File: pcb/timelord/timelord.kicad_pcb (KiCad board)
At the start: 4 copper layers, 65 x 56.5 mm, 16 parts, among them J1 Raspberry_Pi_4, J2 OLED, J3 SMA, J4 EXTERNAL, U1 NEO-F10T

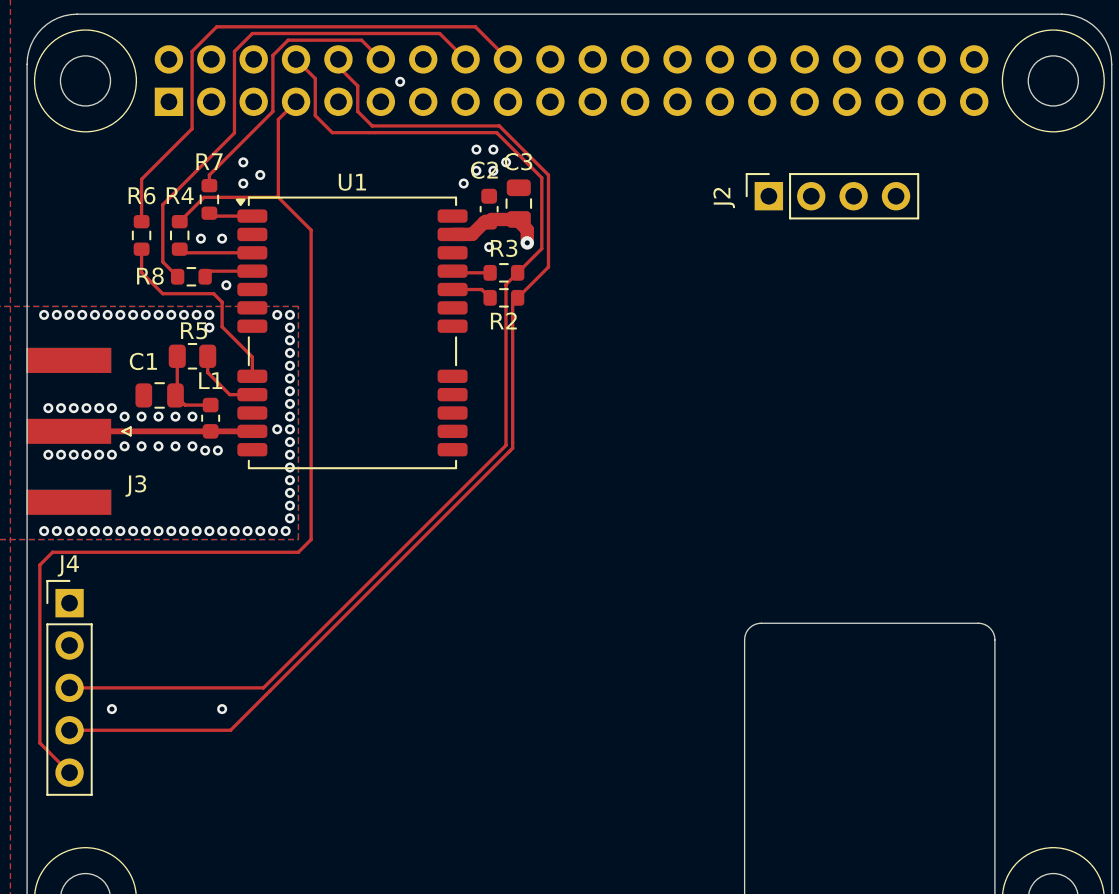
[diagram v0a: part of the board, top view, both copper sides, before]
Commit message: Add external I2C RTC
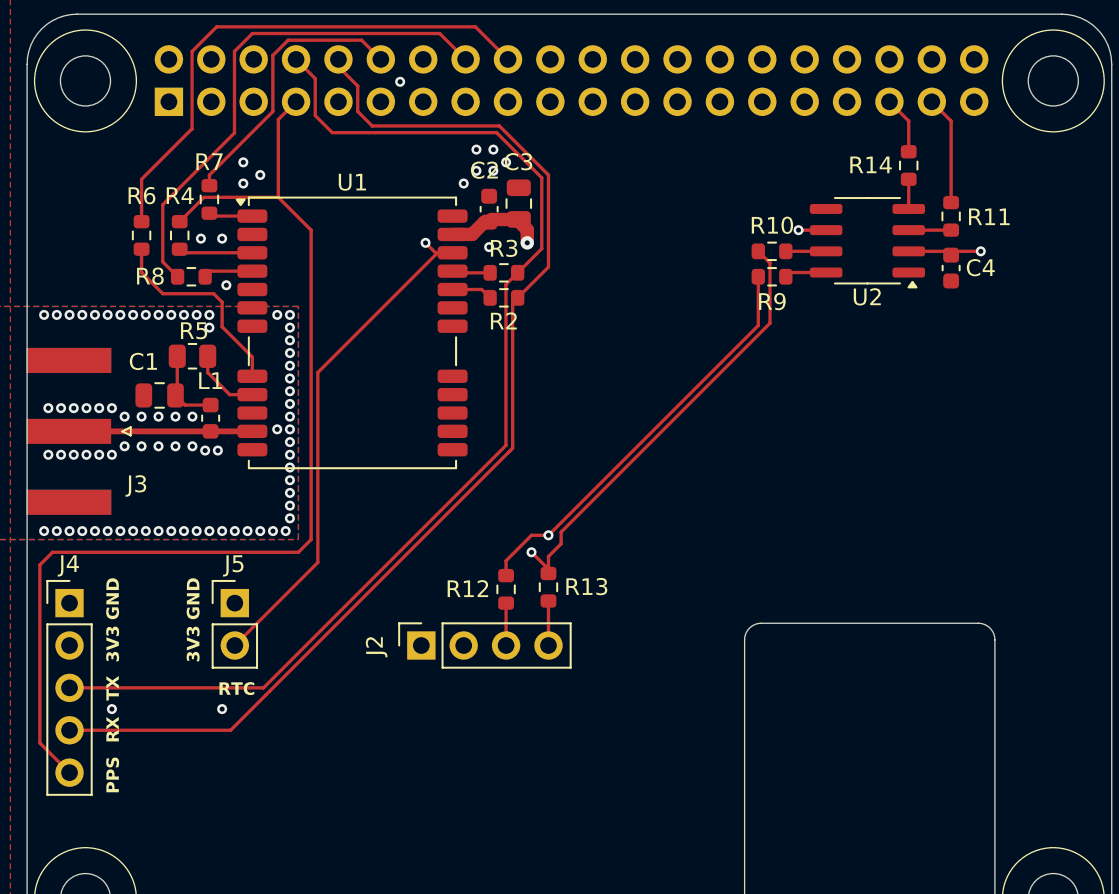
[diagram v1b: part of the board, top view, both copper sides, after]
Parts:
- added C4: 1u, Capacitor_SMD:C_0603_1608Metric, F.Cu at (214.4, 46.2)
- added J5: BCKP_PWR, Connector_PinHeader_2.54mm:PinHeader_1x02_P2.54mm_Vertical, F.Cu at (171.4, 66.3)
- added R10: 33, Resistor_SMD:R_0603_1608Metric, F.Cu at (203.6, 45.2)
- added R11: 33, Resistor_SMD:R_0603_1608Metric, F.Cu at (214.4, 43.1)
- added R12: 33, Resistor_SMD:R_0603_1608Metric, F.Cu at (187.7, 65.5)
- added R13: 33, Resistor_SMD:R_0603_1608Metric, F.Cu at (190.2, 65.3)
- added R14: 33, Resistor_SMD:R_0603_1608Metric, F.Cu at (211.8, 40.1)
- added R9: 33, Resistor_SMD:R_0603_1608Metric, F.Cu at (203.6, 46.7)
- added U2: DS3231MZ, Package_SO:SOIC-8_3.9x4.9mm_P1.27mm, F.Cu at (209.4, 44.6)
- moved J2 34.0 mm to (182.6, 68.8)
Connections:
- J1 pad 35: unconnected-(J1-GPIO19/SPI1_MISO/PCM_FS-Pad35) -> RTC_RESET
- J1 pad 37: unconnected-(J1-GPIO26/SDIO_DAT2-Pad37) -> PPS_RTC
- J2 pad 3: SCL -> Net-(J2-Pin_3)
- J2 pad 4: SDA -> Net-(J2-Pin_4)
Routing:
- net VCC_BCKP: track 0.00 -> 55.7 mm, vias 0 -> 2
- net SCL: track 40.2 -> 58.1 mm, vias 0 -> 1
- net SDA: track 44.9 -> 62.5 mm, vias 0 -> 1
- net PPS_RTC: track 0.00 -> 6.52 mm
- net +3.3V: track 5.88 -> 10.2 mm, vias 1 -> 2
- net RTC_RESET: track 0.00 -> 3.47 mm
- net Net-(J2-Pin_4): track 0.00 -> 2.67 mm
- net Net-(J2-Pin_3): track 0.00 -> 2.54 mm
- net Net-(U2-~{INT}/SQW): track 0.00 -> 2.54 mm
- net Net-(U2-SCL): track 0.00 -> 2.52 mm
- net Net-(U2-SDA): track 0.00 -> 2.42 mm
- net Net-(U2-~{RST}): track 0.00 -> 1.78 mm
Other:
- board text added: "3V3"
- board text added: "GND"
- board text added: "PPS"
- board text added: "RTC"
- board text added: "RX"
- board text added: "TX"

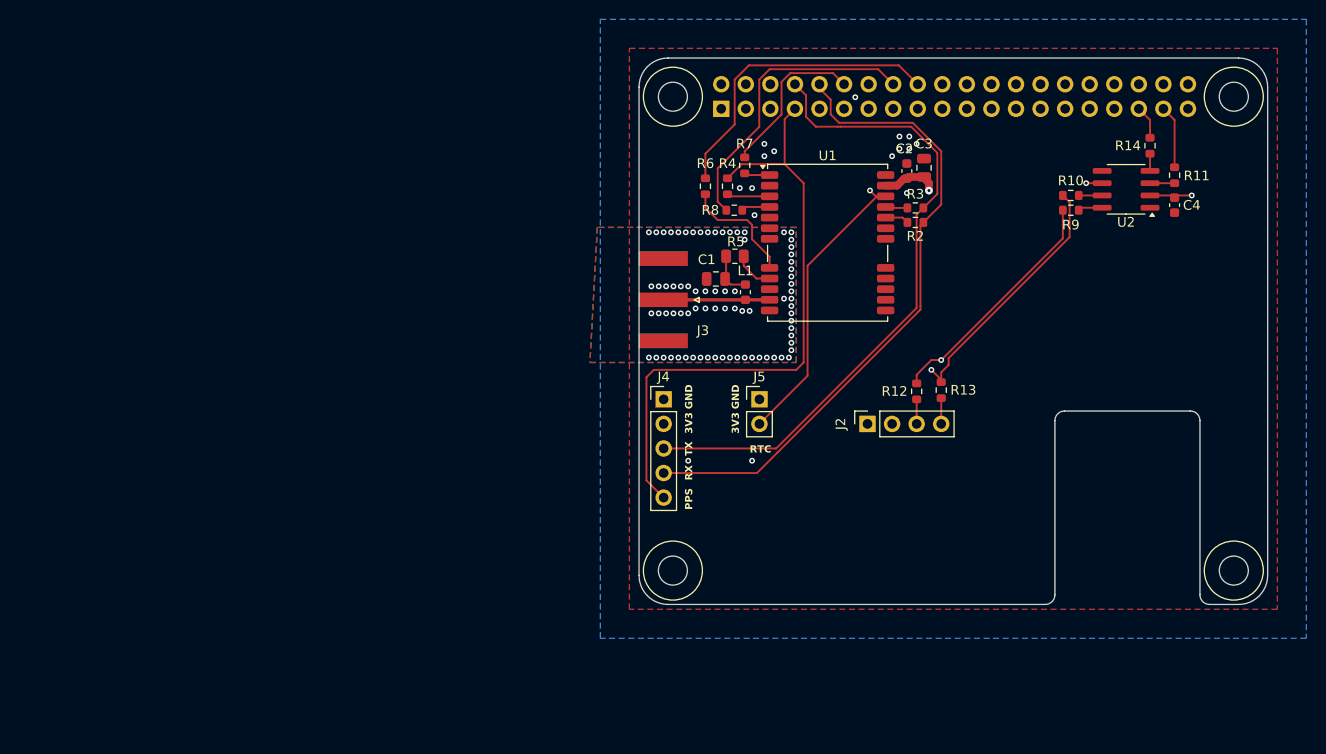
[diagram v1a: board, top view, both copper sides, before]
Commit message: Redesign board edges and add backup power
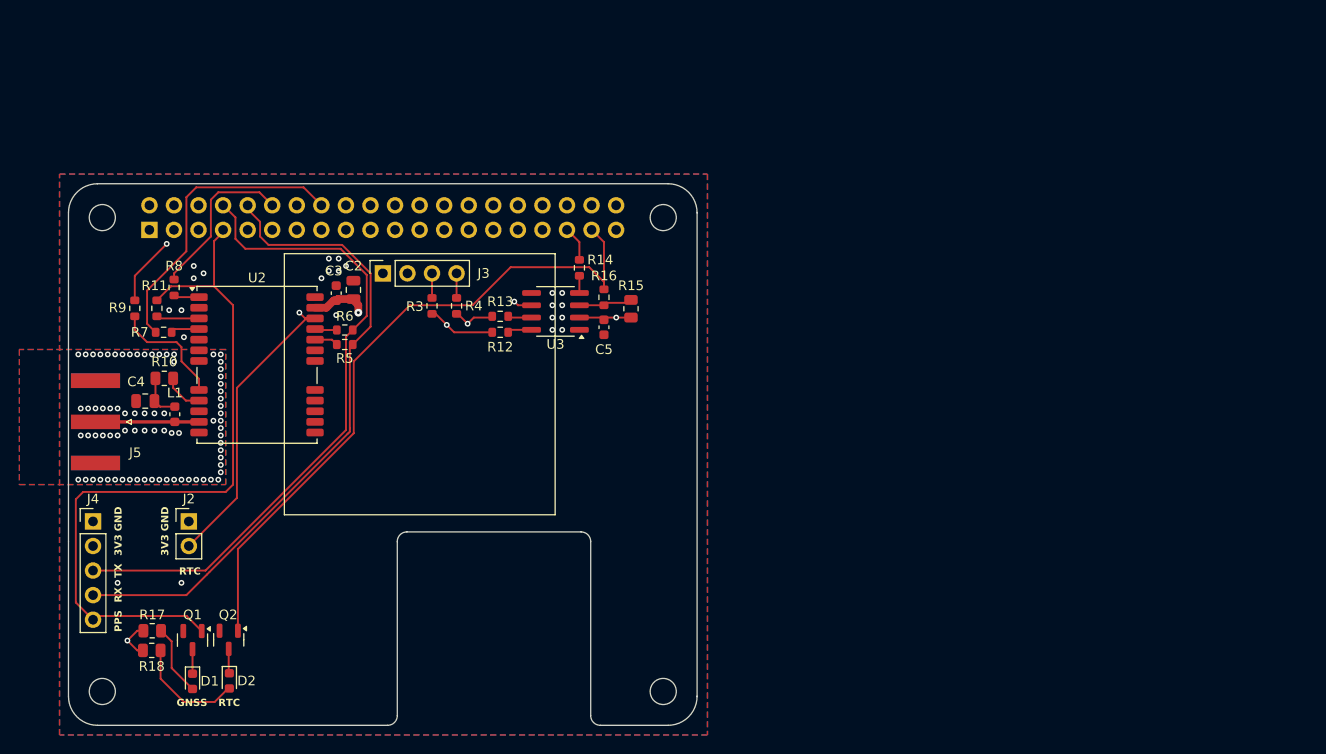
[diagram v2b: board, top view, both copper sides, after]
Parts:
- removed C1: 10n, Capacitor_SMD:C_0805_2012Metric
- removed R2: 33, Resistor_SMD:R_0603_1608Metric
- removed U1: NEO-F10T, RF_GPS:ublox_NEO
- added C5: 1u, Capacitor_SMD:C_0603_1608Metric, F.Cu at (155.4, 58.8)
- added D1: LED, LED_SMD:LED_0603_1608Metric, F.Cu at (112.8, 95.5)
- added D2: LED, LED_SMD:LED_0603_1608Metric, F.Cu at (116.6, 95.4)
- added MH1: MountingHole_2.7mm_M2.5, MountingHole:MountingHole_2.7mm_M2.5, F.Cu at (103.5, 47.5)
- added MH2: MountingHole_2.7mm_M2.5, MountingHole:MountingHole_2.7mm_M2.5, F.Cu at (161.5, 47.5)
- added MH3: MountingHole_2.7mm_M2.5, MountingHole:MountingHole_2.7mm_M2.5, F.Cu at (103.5, 96.5)
- added MH4: MountingHole_2.7mm_M2.5, MountingHole:MountingHole_2.7mm_M2.5, F.Cu at (161.5, 96.5)
- added Q1: BC846, Package_TO_SOT_SMD:SOT-23, F.Cu at (112.8, 91.2)
- added Q2: BC846, Package_TO_SOT_SMD:SOT-23, F.Cu at (116.6, 91.2)
- added R15: 10k, Resistor_SMD:R_0805_2012Metric, F.Cu at (158.2, 56.9)
- added R16: 33, Resistor_SMD:R_0603_1608Metric, F.Cu at (155.4, 55.7)
- added R17: 1k, Resistor_SMD:R_0805_2012Metric, F.Cu at (108.7, 90.2)
- added R18: 1k, Resistor_SMD:R_0805_2012Metric, F.Cu at (108.6, 92.3)
- added U3: DS3231MZ, Package_SO:SOIC-8_3.9x4.9mm_P1.27mm, F.Cu at (150.4, 57.2)
- C2: value 1u -> 22u; footprint Capacitor_SMD:C_0603_1608Metric -> Capacitor_SMD:C_0805_2012Metric
- C3: value 22u -> 1u; footprint Capacitor_SMD:C_0805_2012Metric -> Capacitor_SMD:C_0603_1608Metric
- C4: value 1u -> 10n; footprint Capacitor_SMD:C_0603_1608Metric -> Capacitor_SMD:C_0805_2012Metric
- J1: value Raspberry_Pi_4 -> GPIO
- J2: value OLED -> BCKP_PWR; footprint Connector_PinSocket_2.54mm:PinSocket_1x04_P2.54mm_Vertical -> Connector_PinHeader_2.54mm:PinHeader_1x02_P2.54mm_Vertical
- J3: value SMA -> OLED; footprint Connector_Coaxial:SMA_Amphenol_132289_EdgeMount -> Connector_PinSocket_2.54mm:PinSocket_1x04_P2.54mm_Vertical
- J5: value BCKP_PWR -> SMA; footprint Connector_PinHeader_2.54mm:PinHeader_1x02_P2.54mm_Vertical -> Connector_Coaxial:SMA_Amphenol_132289_EdgeMount
- R10: value 33 -> 10; footprint Resistor_SMD:R_0603_1608Metric -> Resistor_SMD:R_0805_2012Metric
- R5: value 10 -> 33; footprint Resistor_SMD:R_0805_2012Metric -> Resistor_SMD:R_0603_1608Metric
- U2: value DS3231MZ -> NEO-F10T; footprint Package_SO:SOIC-8_3.9x4.9mm_P1.27mm -> RF_GPS:ublox_NEO
- moved C4 108.3 mm to (107.9, 66.5), turned to 180 degrees
- moved R11 106.1 mm to (109.1, 56.9)
- moved R9 97.3 mm to (106.9, 56.9), turned to 90 degrees
- moved R10 95.6 mm to (109.9, 64.1)
- moved U2 91.7 mm to (119.5, 62.7), turned to 0 degrees
- moved J2 70.9 mm to (112.4, 78.9), turned to 0 degrees
- moved J5 68.7 mm to (102.8, 68.6), turned to 180 degrees
- moved R7 62.5 mm to (109.8, 59.4), turned to 0 degrees
- moved C3 62.1 mm to (127.7, 55.3)
- moved J1 60.4 mm to (108.4, 48.8)
- moved R14 60.3 mm to (152.8, 52.7)
- moved J4 60.3 mm to (102.5, 78.9)
- moved L1 60.3 mm to (111.0, 67.8)
- moved C2 58.5 mm to (129.5, 55.0)
- moved R8 58.5 mm to (110.9, 54.7), turned to -90 degrees
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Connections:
- C4 pad 1: +3.3V -> Net-(C4-Pad1)
- J1 pad 11: unconnected-(J1-GPIO17/SPI1_~{CE1}-Pad11) -> /GPIO17
- J1 pad 13: unconnected-(J1-GPIO27/SDIO_DAT3-Pad13) -> /GPIO27
- J1 pad 15: unconnected-(J1-GPIO22/SDIO_CLK-Pad15) -> /GPIO22
- J1 pad 19: unconnected-(J1-MOSI_SPI0/GPIO10-Pad19) -> /GPIO10/SPI0.MOSI
- J1 pad 21: unconnected-(J1-MISO_SPI0/GPIO09-Pad21) -> /GPIO9/SPI0.MISO
- J1 pad 22: unconnected-(J1-GPIO25/SDIO_DAT1-Pad22) -> /GPIO25
- J1 pad 23: unconnected-(J1-SCLK_SPI0/GPIO11-Pad23) -> /GPIO11/SPI0.SCLK
- J1 pad 24: unconnected-(J1-~{CE0}_SPI0/GPIO08-Pad24) -> /GPIO8/SPI0.CE0
- J1 pad 26: unconnected-(J1-~{CE1}_SPI0/GPIO07-Pad26) -> /GPIO7/SPI0.CE1
- J1 pad 27: unconnected-(J1-ID_SD_I2C0/GPIO00-Pad27) -> /ID_SDA
- J1 pad 28: unconnected-(J1-ID_SC_I2C0/GPIO01-Pad28) -> /ID_SCL
- J1 pad 29: unconnected-(J1-GPCLK1/GPIO05-Pad29) -> /GPIO5
- J1 pad 31: unconnected-(J1-GPCLK2/GPIO06-Pad31) -> /GPIO6
- J1 pad 32: unconnected-(J1-GPIO12/PWM0-Pad32) -> /GPIO12/PWM0
- J1 pad 33: unconnected-(J1-GPIO13/PWM1-Pad33) -> /GPIO13/PWM1
- J1 pad 36: unconnected-(J1-GPIO16/SPI1_~{CE2}-Pad36) -> /GPIO16
- J1 pad 38: unconnected-(J1-GPIO20/SPI1_MOSI/PCM_DIN/PWM1-Pad38) -> /GPIO20/PCM.DIN
- J1 pad 40: unconnected-(J1-GPIO21/SPI1_SCLK/PCM_DOUT-Pad40) -> /GPIO21/PCM.DOUT
- J2 pad 2: +3.3V -> VCC_BCKP
- J3 pad 1: Net-(J3-In) -> GND
- J3 pad 2: GND -> +3.3V
- J5 pad 1: GND -> Net-(J5-In)
- J5 pad 2: VCC_BCKP -> GND
- L1 pad 1: Net-(C1-Pad1) -> Net-(C4-Pad1)
- L1 pad 2: Net-(J3-In) -> Net-(J5-In)
- R10 pad 1: Net-(U2-SDA) -> Net-(U2-VCC_RF)
- R10 pad 2: SDA -> Net-(C4-Pad1)
- R11 pad 1: PPS_RTC -> PPS
- R12 pad 2: Net-(J2-Pin_3) -> Net-(U3-SCL)
- R13 pad 1: Net-(J2-Pin_4) -> Net-(U3-SDA)
- R14 pad 1: Net-(U2-~{RST}) -> Net-(U3-~{RST})
- R3 pad 1: Net-(U1-RXD) -> SCL
- R3 pad 2: UART_TX -> Net-(J3-Pin_3)
- R4 pad 1: PPS -> Net-(J3-Pin_4)
- R4 pad 2: Net-(U1-TIMEPULSE) -> SDA
- R5 pad 1: Net-(U1-VCC_RF) -> UART_RX
- R5 pad 2: Net-(C1-Pad1) -> Net-(U2-TXD)
- R6 pad 1: Net-(U1-~{RESET}) -> Net-(U2-RXD)
- R6 pad 2: RESET -> UART_TX
- R7 pad 1: SAFEBOOT -> EXTINT
- R7 pad 2: Net-(U1-SAFEBOOT_N) -> Net-(U2-EXTINT)
- R8 pad 1: EXTINT -> SAFEBOOT
- R8 pad 2: Net-(U1-EXTINT) -> Net-(U2-SAFEBOOT_N)
- R9 pad 1: SCL -> Net-(U2-~{RESET})
- R9 pad 2: Net-(U2-SCL) -> RESET
- U2 pad 1: unconnected-(U2-32KHZ-Pad1) -> Net-(U2-SAFEBOOT_N)
- U2 pad 2: +3.3V -> unconnected-(U2-RESERVED-Pad2)
- U2 pad 4: Net-(U2-~{RST}) -> Net-(U2-EXTINT)
- U2 pad 5: GND -> unconnected-(U2-RESERVED-Pad5)
- U2 pad 6: VCC_BCKP -> unconnected-(U2-RESERVED-Pad6)
- U2 pad 7: Net-(U2-SDA) -> unconnected-(U2-RESERVED-Pad7)
- U2 pad 8: Net-(U2-SCL) -> Net-(U2-~{RESET})
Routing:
- net PPS_RTC: track 6.52 -> 70.6 mm
- net SDA: track 62.5 -> 39.9 mm
- net SCL: track 58.1 -> 37.9 mm
- net +3.3V: track 10.2 -> 27.0 mm, vias 2 -> 3
- net Net-(U1-~{RESET}): track 12.2 -> 0.00 mm
- net Net-(U2-~{RESET}): track 0.00 -> 12.2 mm
- net PPS: track 64.1 -> 76.1 mm
- net Net-(D2-A): track 0.00 -> 11.5 mm
- net Net-(J5-In): track 0.00 -> 11.0 mm
- net Net-(J3-In): track 11.0 -> 0.00 mm
- net Net-(D1-A): track 0.00 -> 7.37 mm
- net Net-(U3-~{INT}/SQW): track 0.00 -> 5.56 mm
- net Net-(C4-Pad1): track 0.00 -> 4.74 mm
- net Net-(C1-Pad1): track 4.74 -> 0.00 mm
- net Net-(U1-TIMEPULSE): track 4.44 -> 0.00 mm
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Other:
- board size 65 x 56.5 mm -> 65 x 56 mm
- board text added: "GNSS"
- board text added: "PoE"
- board text added: "RJ45"
- board text added: "USB"

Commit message: Cosmetic changes
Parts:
- added JP1: VCC_BCPK_JMPR, Jumper:SolderJumper-2_P1.3mm_Open_TrianglePad1.0x1.5mm, B.Cu at (107.9, 81.5)
- moved C2 0.25 mm to (129.5, 55.2)
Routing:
- net +3.3V: track 27.0 -> 32.9 mm
- net VCC_BCKP: track 56.0 -> 58.5 mm
- net GND: vias 101 -> 99
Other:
- board text added: "3V3 VCC_BCKP"

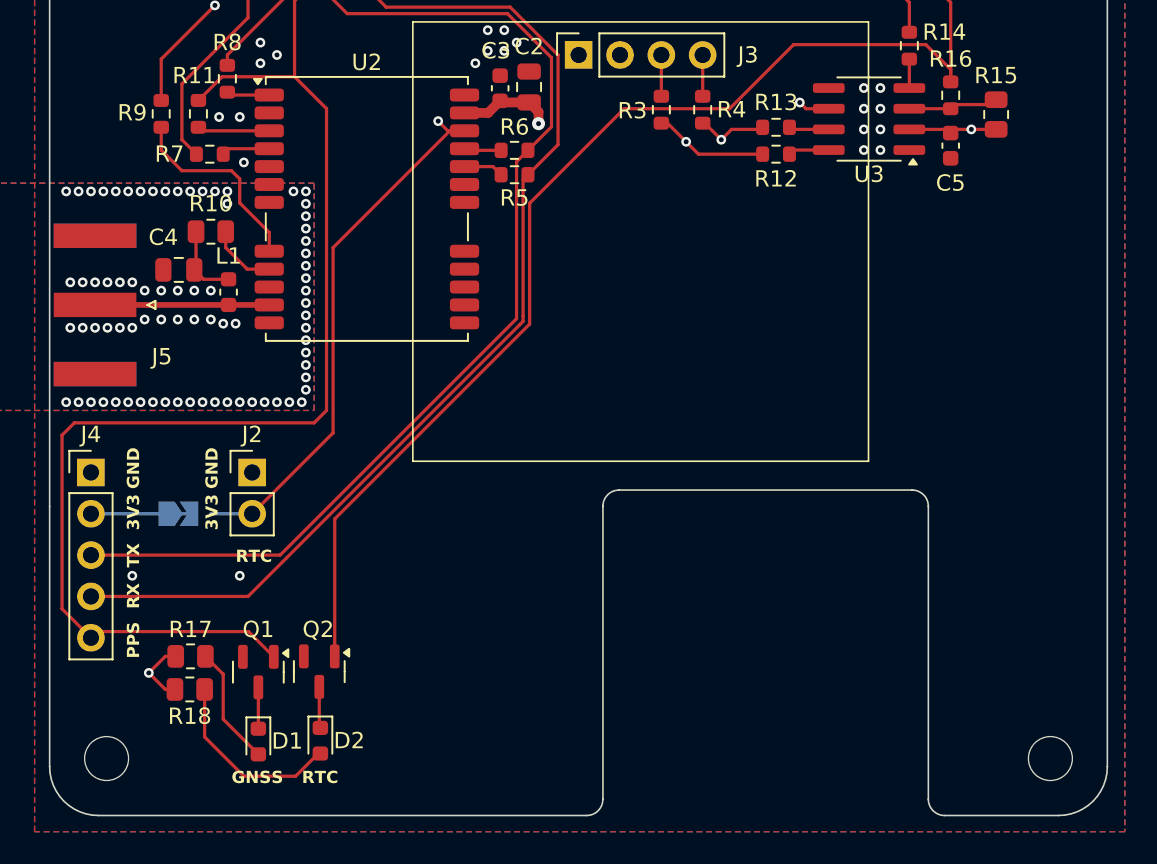
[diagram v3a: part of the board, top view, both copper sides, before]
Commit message: Make rounded corners more rounded
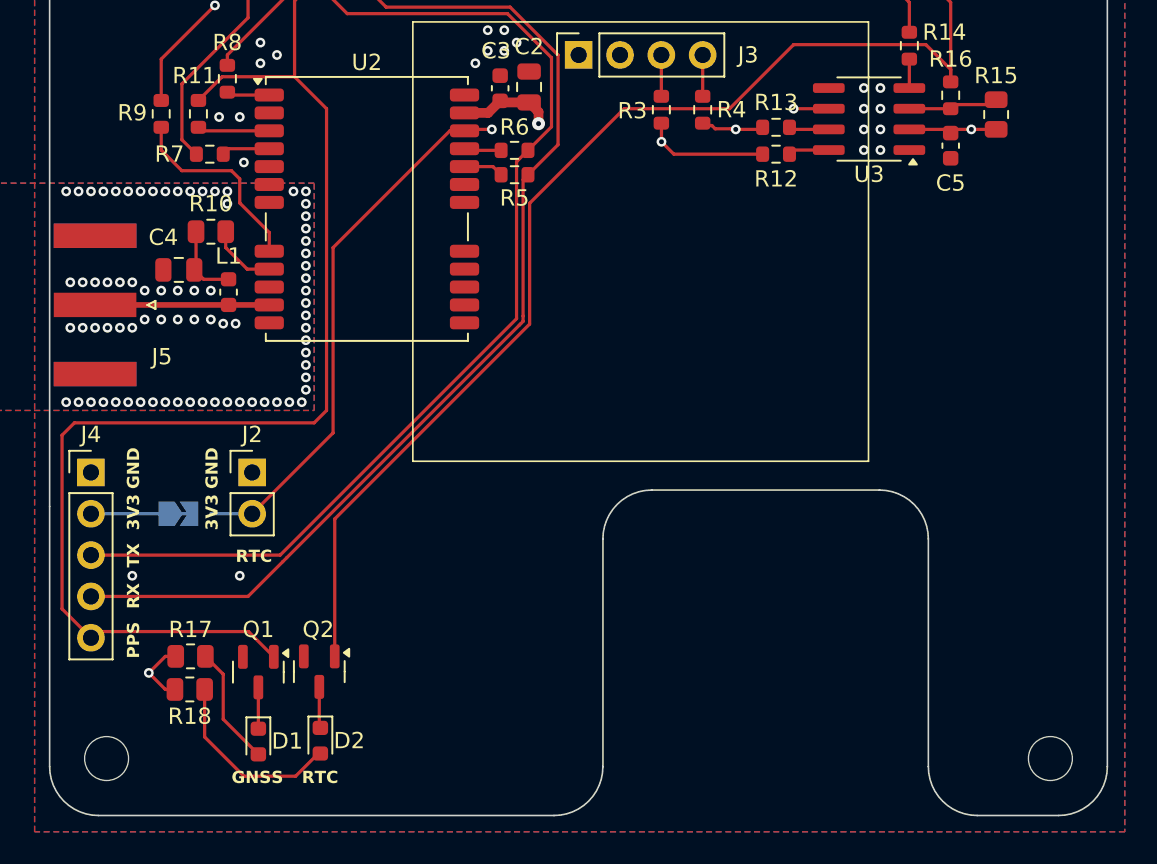
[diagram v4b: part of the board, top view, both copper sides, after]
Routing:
- net VCC_BCKP: track 58.5 -> 55.0 mm
- net SCL: track 37.9 -> 37.0 mm
- net SDA: track 39.9 -> 40.6 mm
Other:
- outline, holes or cut-outs redrawn
